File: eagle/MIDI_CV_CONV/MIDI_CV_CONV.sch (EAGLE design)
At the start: 36 parts, among them CN1 PWR9V, IC1 MCP4922, IC2 TLP552, IC3 74HC541N, IC4 TD62003

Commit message: Add: Board Design
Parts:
- added JP8: PGM_SW, pinhead:PINHD-1X2
- C2: device rcl:C-EU025-024X044 -> rcl:C-EU050-024X044
- JP6: value CHK -> TP_CHK
- LED1, LED2, LED3, LED4, LED5, LED6: value (none) -> GREEN
- R10, R11, R12, R7, R8, R9: device rcl:R-EU_0207/7 -> rcl:R-EU_0207/2V
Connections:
- removed net N$15 (its old number): IC3A.A2, IC4.I1, U$1.D2
- removed net N$31: LED2.C, R8.1
- removed net N$32: LED3.C, R9.1
- removed net N$33: LED4.C, R10.1
- removed net N$34: LED5.C, R11.1
- removed net N$35: LED6.C, R12.1
- removed net N$36: IC4.O1, R7.2
- new net GATE0: IC3A.A2, IC4.I1, U$1.D7
- new net GATE1: IC3A.A3, IC4.I2, U$1.D6
- new net GATE2: IC3A.A4, IC4.I3, U$1.D5
- new net GATE3: IC3A.A5, IC4.I4, U$1.D4
- new net GATE4: IC3A.A6, IC4.I5, U$1.D3
- new net GATE5: IC3A.A7, IC4.I6, U$1.D2
- new net N$28: LED6.C, R12.2
- new net N$3: IC2.OUT, JP8.1, R2.1
- net +9V: now also CN1.1; no longer CN1.2
- net GND: now also CN1.2; no longer CN1.1
- net N$16: now also LED1.C, R7.2; no longer IC3A.A3, IC4.I2, U$1.D3
- net N$17: now also LED2.C, R8.2; no longer IC3A.A4, IC4.I3, U$1.D4
- net N$18: now also LED3.C, R9.2; no longer IC3A.A5, IC4.I4, U$1.D5
- net N$19: now also LED4.C, R10.2; no longer IC3A.A6, IC4.I5, U$1.D6
- net N$2: now also JP8.2; no longer IC2.OUT, R2.1
- net N$20: now also LED5.C, R11.2; no longer IC3A.A7, IC4.I6, U$1.D7
- net N$30: now also IC4.O1; no longer LED1.C
- net N$37: now also R8.1; no longer R8.2
- net N$38: now also R9.1; no longer R9.2
- net N$39: now also R10.1; no longer R10.2
- net N$40: now also R11.1; no longer R11.2
- net N$41: now also R12.1; no longer R12.2
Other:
- moved on the sheet: CN1, JP6, R10, R11, R12, R7, R8, R9

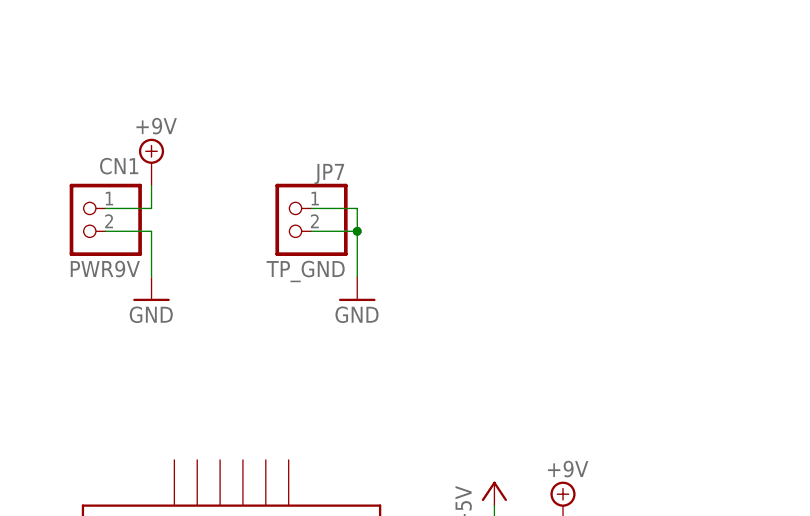
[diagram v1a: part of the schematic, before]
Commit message: Add: 5V Power Supply
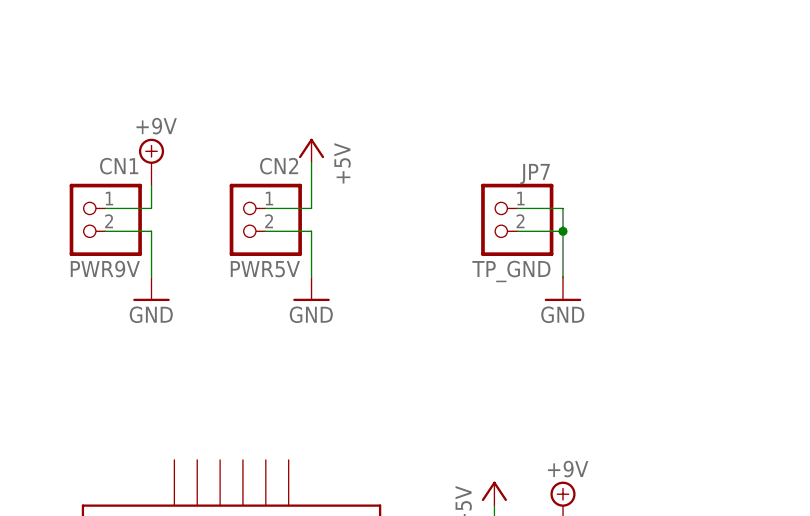
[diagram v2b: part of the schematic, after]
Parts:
- added CN2: PWR5V, jst-xh:B2B-XH-A
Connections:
- net +5V: now also CN2.1
- net GND: now also CN2.2
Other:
- moved on the sheet: JP7
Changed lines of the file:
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@@
 <part name="JP8" library="pinhead" library_urn="urn:adsk.eagle:library:325" deviceset="PINHD-1X2" device="" package3d_urn="urn:adsk.eagle:package:22435/2" value="PGM_SW"/>
 <part name="JP6" library="pinhead" library_urn="urn:adsk.eagle:library:325" deviceset="PINHD-1X1" device="" package3d_urn="urn:adsk.eagle:package:22485/2" value="TP_CHK"/>
+<part name="CN2" library="jst-xh" deviceset="B2B-XH-A" device="" value="PWR5V"/>
+<part name="P+10" library="supply1" library_urn="urn:adsk.eagle:library:371" deviceset="+5V" device=""/>
+<part name="GND14" library="supply1" library_urn="urn:adsk.eagle:library:371" deviceset="GND" device=""/>
 </parts>
 <sheets>
@@
 <instance part="GND12" gate="1" x="83.82" y="35.56"/>
 <instance part="P+9" gate="1" x="12.7" y="71.12"/>
-<instance part="JP7" gate="G$1" x="137.16" y="147.32" rot="MR0"/>
-<instance part="GND13" gate="1" x="144.78" y="139.7"/>
+<instance part="JP7" gate="G$1" x="160.02" y="147.32" rot="MR0"/>
+<instance part="GND13" gate="1" x="167.64" y="139.7"/>
 <instance part="FRAME1" gate="G$1" x="0" y="0"/>
 <instance part="JP8" gate="G$1" x="93.98" y="124.46"/>
 <instance part="JP6" gate="G$1" x="109.22" y="48.26"/>
+<instance part="CN2" gate="G$1" x="134.62" y="149.86" rot="MR0"/>
+<instance part="P+10" gate="1" x="139.7" y="157.48" rot="MR0"/>
+<instance part="GND14" gate="1" x="139.7" y="139.7"/>
 </instances>
 <busses>
@@
 <junction x="12.7" y="60.96"/>
 </segment>
+<segment>
+<pinref part="CN2" gate="G$1" pin="1"/>
+<wire x1="134.62" y1="149.86" x2="139.7" y2="149.86" width="0.1524" layer="91"/>
+<pinref part="P+10" gate="1" pin="+5V"/>
+<wire x1="139.7" y1="149.86" x2="139.7" y2="154.94" width="0.1524" layer="91"/>
+</segment>
 </net>
 <net name="N$4" class="0">
@@
 <segment>
 <pinref part="GND13" gate="1" pin="GND"/>
-<wire x1="144.78" y1="142.24" x2="144.78" y2="147.32" width="0.1524" layer="91"/>
+<wire x1="167.64" y1="142.24" x2="167.64" y2="147.32" width="0.1524" layer="91"/>
 <pinref part="JP7" gate="G$1" pin="1"/>
-<wire x1="144.78" y1="147.32" x2="144.78" y2="149.86" width="0.1524" layer="91"/>
-<wire x1="144.78" y1="149.86" x2="139.7" y2="149.86" width="0.1524" layer="91"/>
+<wire x1="167.64" y1="147.32" x2="167.64" y2="149.86" width="0.1524" layer="91"/>
+<wire x1="167.64" y1="149.86" x2="162.56" y2="149.86" width="0.1524" layer="91"/>
 <pinref part="JP7" gate="G$1" pin="2"/>
-<wire x1="139.7" y1="147.32" x2="144.78" y2="147.32" width="0.1524" layer="91"/>
-<junction x="144.78" y="147.32"/>
+<wire x1="162.56" y1="147.32" x2="167.64" y2="147.32" width="0.1524" layer="91"/>
+<junction x="167.64" y="147.32"/>
 </segment>
 <segment>
@@
 <junction x="83.82" y="43.18"/>
 </segment>
-</net>
+<segment>
+<pinref part="CN2" gate="G$1" pin="2"/>
+<wire x1="134.62" y1="147.32" x2="139.7" y2="147.32" width="0.1524" layer="91"/>
+<pinref part="GND14" gate="1" pin="GND"/>
+<wire x1="139.7" y1="147.32" x2="139.7" y2="142.24" width="0.1524" layer="91"/>
+</segment>
+</net>
